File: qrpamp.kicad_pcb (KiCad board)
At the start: 2 copper layers, 144.8 x 82.6 mm, 110 parts, among them K1 BAND3_IN, K2 BAND2_IN, K3 BAND1_IN, K4 BAND3_OUT, K5 BAND2_OUT, K6 BAND1_OUT, K7 ANT_RLY, P1 PWR, P2 PWR_SW, P3 SWD, P4 ANT, P5 RADIO, P6 PTT_IN, P7 Thumb-Joystick, Q1 MMBT6427, Q2 MMBF170, Q3 IRF510, Q4 IRF510, SW1 SW_PUSH, T1 8:8, T2 8:8, T3 2:3, T4 12:1, T5 1:12, U1 LM7805, U2 LM3940, U3 LCD-2x16, U4 STM32F401xB/C-LQFP

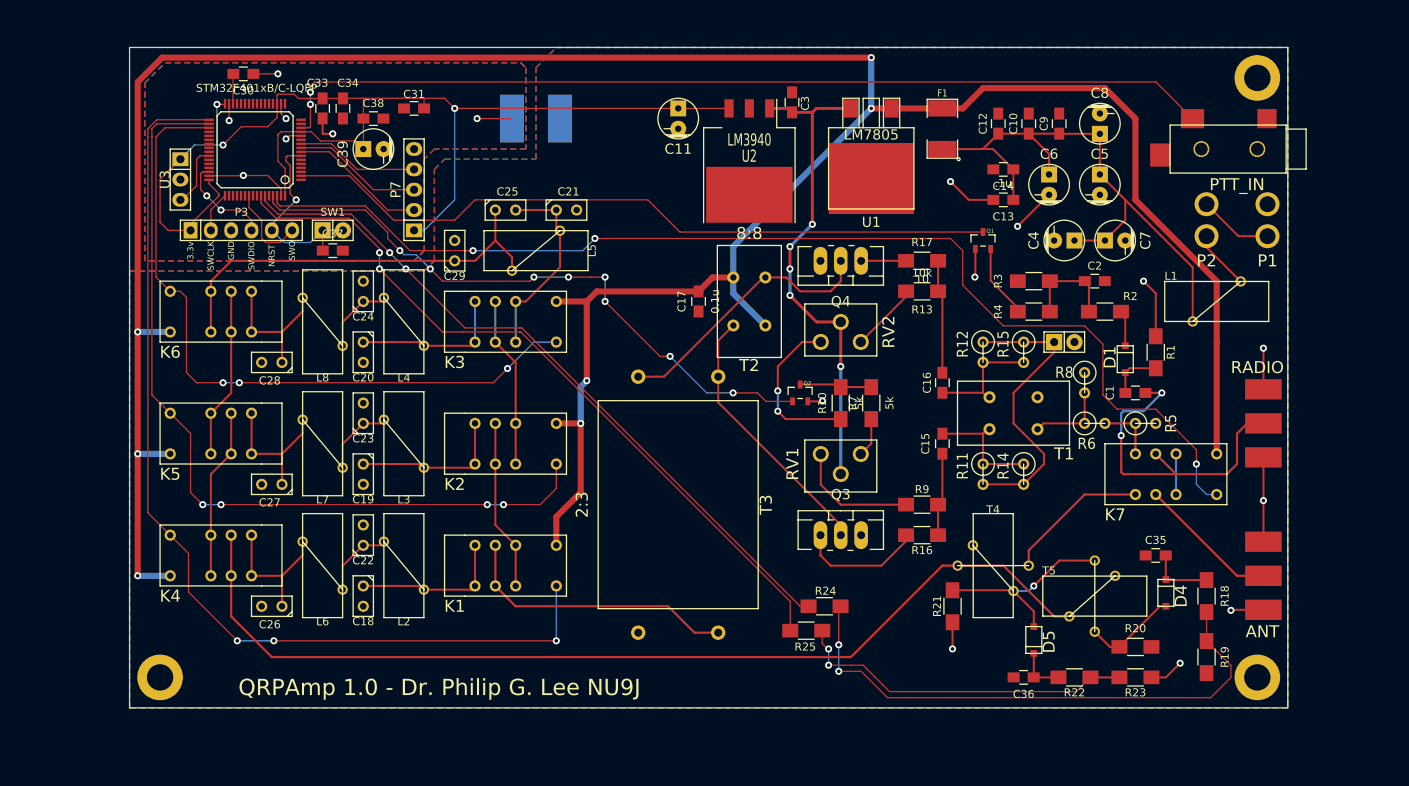
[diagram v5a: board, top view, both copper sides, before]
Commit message: Fixed issues found with test board
- Added MOSFETs to relay switch lines from MCU
- Reconnected SWR in/out to actual ADC pins
- Changed LM3940 footprint to SOT223
- Added 4th mounting hole
- Swapped joystick for nav button
- Extended pads of STM32F401 for easier soldering
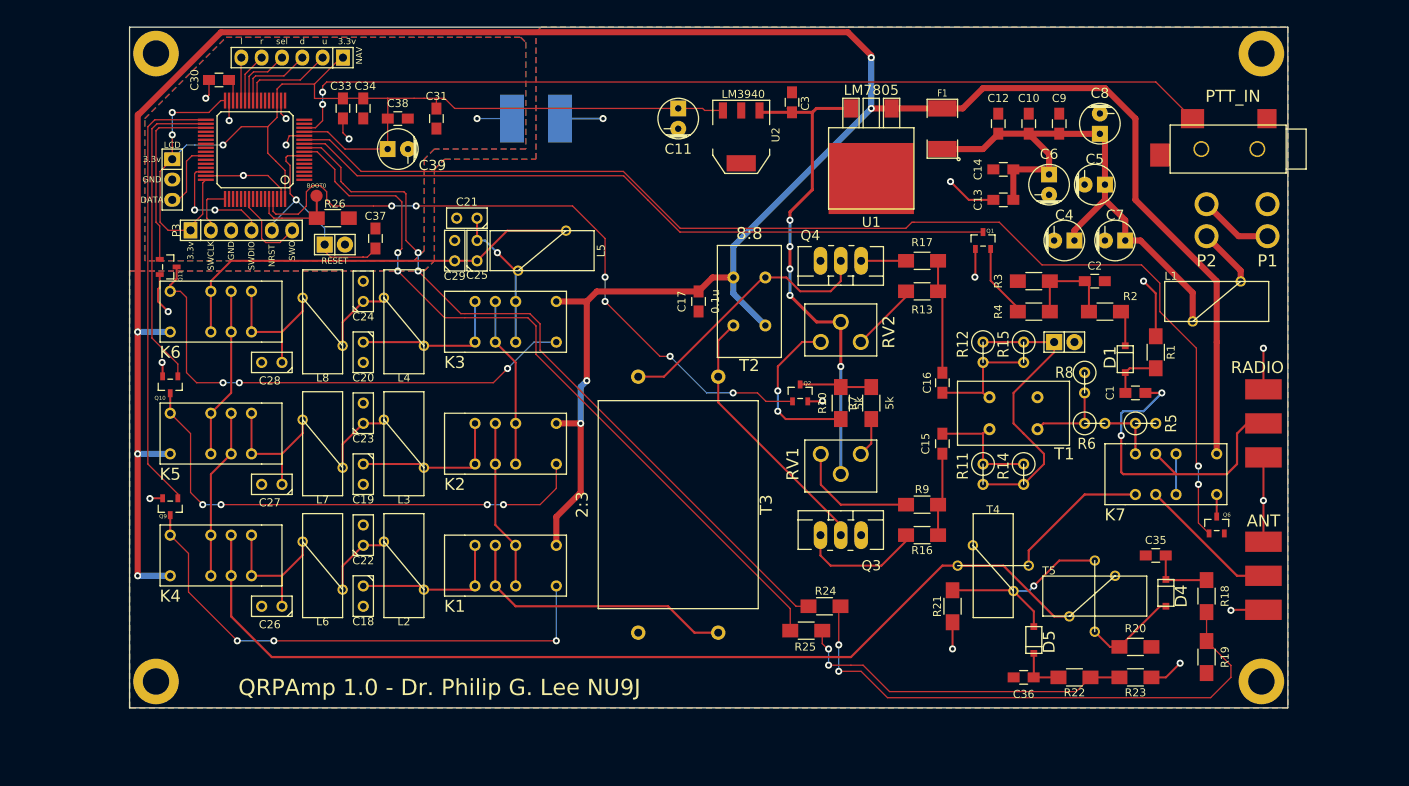
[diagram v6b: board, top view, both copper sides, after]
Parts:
- removed the Mounting Hole at (86.4, 128.3)
- removed the Mounting Hole at (223.5, 128.3)
- removed the Mounting Hole at (223.5, 53.3)
- added Mounting Hole: VAL**, nu9j-footprints:MountingHole4-40, F.Cu at (224.0, 53.3)
- added Mounting Hole: VAL**, nu9j-footprints:MountingHole4-40, F.Cu at (224.0, 128.8)
- added Mounting Hole: VAL**, nu9j-footprints:MountingHole4-40, F.Cu at (86.4, 128.8)
- added Mounting Hole: VAL**, nu9j-footprints:MountingHole4-40, F.Cu at (85.9, 50.3)
- added P8: NAV_BUTTON, Pin_Headers:Pin_Header_Straight_1x06, F.Cu at (102.9, 50.8)
- added Q10: MMBF170, nu9j-footprints:sot23-DGS, F.Cu at (87.6, 91.7)
- added Q11: MMBF170, nu9j-footprints:sot23-DGS, F.Cu at (87.4, 77.0)
- added Q6: MMBF170, nu9j-footprints:sot23-DGS, F.Cu at (218.4, 109.2)
- added Q9: MMBF170, nu9j-footprints:sot23-DGS, F.Cu at (87.6, 106.9)
- added R26: 10k, Resistors_SMD:R_1206_HandSoldering, F.Cu at (108.0, 70.9)
- P7: value Thumb-Joystick -> TP; footprint Pin_Headers:Pin_Header_Straight_1x05 -> Measurement_Points:Measurement_Point_Round-SMD-Pad_Small
- U2: footprint nu9j-footprints:TO-263_VIVOGND -> SMD_Packages:SOT-223
- moved C21 12.5 mm to (124.7, 70.9), turned to 180 degrees
- moved P7 12.2 mm to (105.9, 68.1)
- moved C25 6.20 mm to (126.0, 74.9), turned to 90 degrees
- moved C37 5.55 mm to (113.3, 73.4), turned to 90 degrees
- moved U2 3.70 mm to (159.0, 60.7)
- moved C30 3.14 mm to (93.7, 53.6), turned to 0 degrees
- moved C31 3.07 mm to (120.9, 58.4), turned to 270 degrees
- moved C38 3.05 mm to (116.1, 58.4)
- moved C39 3.05 mm to (116.1, 62.2)
- moved C34 2.54 mm to (111.8, 57.1)
- moved C33 2.54 mm to (109.2, 57.1)
- moved SW1 1.80 mm to (108.2, 74.2)
- moved U3 1.02 mm to (87.9, 66.0)
- moved L5 0.76 mm to (134.1, 74.9), turned to 90 degrees
- moved C5 0.64 mm to (203.2, 66.7), turned to 90 degrees
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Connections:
- K1 pad 12: /Band Filters/bandfilter_3sel -> /Band Filters/band3_sel
- K2 pad 12: /Band Filters/bandfilter_2sel -> /Band Filters/band2_sel
- K3 pad 12: /Band Filters/bandfilter_1sel -> /Band Filters/band1_sel
- K4 pad 12: /Band Filters/bandfilter_3sel -> /Band Filters/band3_sel
- K5 pad 12: /Band Filters/bandfilter_2sel -> /Band Filters/band2_sel
- K6 pad 12: /Band Filters/bandfilter_1sel -> /Band Filters/band1_sel
- K7 pad 12: /RF In/Out/ant_sw_rly -> Net-(K7-Pad12)
- P7 pad 1: +3.3V -> Net-(P7-Pad1)
- U4 pad 10: Net-(P7-Pad4) -> /Microcontroller/mcu_rfdet
- U4 pad 11: Net-(U4-Pad11) -> /RF In/Out/ant_sw_rly
- U4 pad 2: /Microcontroller/mcu_rfdet -> Net-(U4-Pad2)
- U4 pad 24: Net-(U4-Pad24) -> /Microcontroller/nav_up
- U4 pad 25: Net-(U4-Pad25) -> /Microcontroller/nav_down
- U4 pad 26: Net-(U4-Pad26) -> /Microcontroller/nav_select
- U4 pad 27: Net-(U4-Pad27) -> /Microcontroller/nav_right
- U4 pad 28: Net-(U4-Pad28) -> /Microcontroller/nav_left
- U4 pad 58: Net-(R24-Pad1) -> Net-(U4-Pad58)
- U4 pad 59: Net-(R25-Pad2) -> Net-(U4-Pad59)
- U4 pad 60: Net-(U4-Pad60) -> Net-(P7-Pad1)
- U4 pad 62: /RF In/Out/ant_sw_rly -> Net-(U4-Pad62)
- U4 pad 8: Net-(P7-Pad2) -> Net-(R24-Pad1)
- U4 pad 9: Net-(P7-Pad3) -> Net-(R25-Pad2)
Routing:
- net /Band Filters/bandfilter_3sel: track 123.5 -> 56.0 mm, vias 3 -> 0
- net /Band Filters/band3_sel: track 0.00 -> 65.9 mm, vias 0 -> 3
- net /Band Filters/bandfilter_2sel: track 105.1 -> 39.7 mm, vias 4 -> 0
- net /Band Filters/bandfilter_1sel: track 88.1 -> 23.0 mm, vias 3 -> 0
- net /Band Filters/band1_sel: track 0.00 -> 64.3 mm, vias 0 -> 3
- net /Band Filters/band2_sel: track 0.00 -> 63.7 mm, vias 0 -> 4
- net Net-(P7-Pad2): track 17.1 -> 0.00 mm
- net Net-(P7-Pad3): track 16.3 -> 0.00 mm
- net Net-(P7-Pad4): track 15.5 -> 0.00 mm
- net /Microcontroller/nav_up: track 0.00 -> 12.9 mm
- net Net-(P7-Pad1): track 0.00 -> 12.0 mm
- net /Microcontroller/nav_down: track 0.00 -> 11.3 mm
- net GND: track 52.2 -> 60.7 mm, vias 10 -> 13
- net /Microcontroller/nav_select: track 0.00 -> 8.11 mm
- net /Amplifier/amp_on: track 78.8 -> 85.5 mm, vias 8 -> 6
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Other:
- board size 144.8 x 82.6 mm -> 144.8 x 85.1 mm
- board text added: "BOOT0"
- board text added: "DATA"
- board text added: "LCD"
- board text added: "NAV"
- board text added: "RESET"
- board text added: "d"
- board text added: "l"
- board text added: "r"
- board text added: "sel"
- board text added: "u"

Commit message: Off to the fab!
Had to fix an issue where the GND-DGND bead was not putting solder
mask on the bottom pads.
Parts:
- L9: moved to B.Cu
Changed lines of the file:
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@@
     (links 250)
     (no_connects 0)
-    (area 82.474999 46.914999 227.405001 132.155001)
+    (area 80.118238 43.813 229.949001 132.155001)
     (thickness 1.6)
     (drawings 24)
@@
     (mod_text_size 1.5 1.5)
     (mod_text_width 0.15)
-    (pad_size 5.7 5.7)
-    (pad_drill 3.3)
+    (pad_size 2.99974 5.99948)
+    (pad_drill 0)
     (pad_to_mask_clearance 0.2)
     (aux_axis_origin 0 0)
@@
     (visible_elements FFFFFF7F)
     (pcbplotparams
-      (layerselection 0x00030_80000001)
+      (layerselection 0x000f0_80000001)
       (usegerberextensions false)
       (excludeedgelayer true)
@@
       (outputformat 1)
       (mirror false)
-      (drillshape 1)
+      (drillshape 0)
       (scaleselection 1)
-      (outputdirectory ""))
+      (outputdirectory gerber/))
   )
   (net 0 "")
@@
     (add_net "Net-(U3-Pad3)")
   )
+  (module nu9j-footprints:WE-SUCKW (layer B.Cu)
+    (at 133.35 58.42 180)
+    (fp_text reference L9 (at 0 5.00126 180) (layer B.SilkS)
+      (effects (font (thickness 0.3048)) (justify mirror))
+    )
+    (fp_text value BEAD (at 0 -5.00126 180) (layer B.SilkS)
+      (effects (font (thickness 0.3048)) (justify mirror))
+    )
+    (fp_line (start -5.99948 2.49936) (end -5.99948 -2.49936) (layer B.SilkS) (width 0.381))
+    (fp_line (start -5.99948 -2.49936) (end 5.99948 -2.49936) (layer B.SilkS) (width 0.381))
+    (fp_line (start 5.99948 -2.49936) (end 5.99948 2.49936) (layer B.SilkS) (width 0.381))
+    (fp_line (start 5.99948 2.49936) (end -5.99948 2.49936) (layer B.SilkS) (width 0.381))
+    (pad 1 smd rect (at -2.99974 0 180) (size 2.99974 5.99948) (layers B.Cu B.Paste B.Mask)
+      (net 3 GND))
+    (pad 2 smd rect (at 2.99974 0 180) (size 2.99974 5.99948) (layers B.Cu B.Paste B.Mask)
+      (net 88 DGND))
+  )
   (module nu9j-footprints:LQFP64 (layer F.Cu)
     (at 103.984 66.068143 90)
@@
       (net 34 "/Band Filters/bandfilter_out"))
   )
-  (module nu9j-footprints:WE-SUCKW (layer F.Cu)
-    (at 133.35 58.42 180)
-    (fp_text reference L9 (at 0 -5.00126 180) (layer B.SilkS)
-      (effects (font (thickness 0.3048)) (justify mirror))
-    )
-    (fp_text value BEAD (at 0 5.00126 180) (layer B.SilkS)
-      (effects (font (thickness 0.3048)) (justify mirror))
-    )
-    (fp_line (start -5.99948 -2.49936) (end -5.99948 2.49936) (layer B.SilkS) (width 0.381))
-    (fp_line (start -5.99948 2.49936) (end 5.99948 2.49936) (layer B.SilkS) (width 0.381))
-    (fp_line (start 5.99948 2.49936) (end 5.99948 -2.49936) (layer B.SilkS) (width 0.381))
-    (fp_line (start 5.99948 -2.49936) (end -5.99948 -2.49936) (layer B.SilkS) (width 0.381))
-    (pad 1 smd rect (at -2.99974 0 180) (size 2.99974 5.99948) (layers B.Cu F.Paste F.Mask)
-      (net 3 GND))
-    (pad 2 smd rect (at 2.99974 0 180) (size 2.99974 5.99948) (layers B.Cu F.Paste F.Mask)
-      (net 88 DGND))
-  )
   (module nu9j-footprints:TOROID-50 (layer F.Cu)

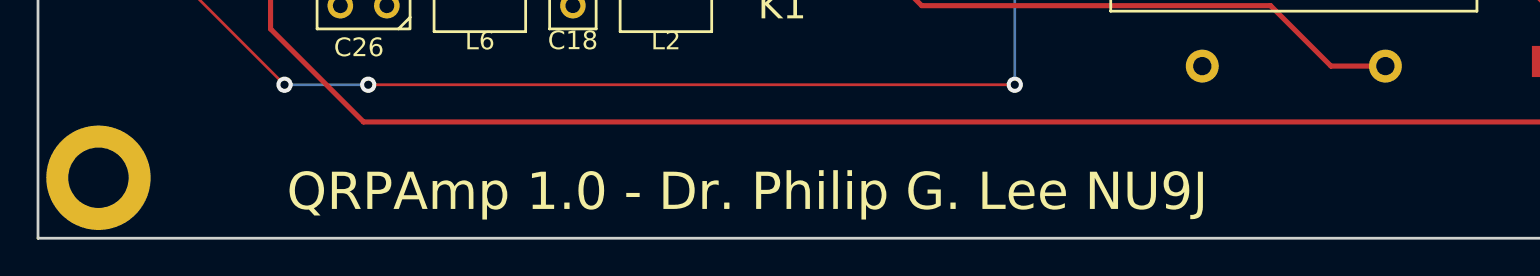
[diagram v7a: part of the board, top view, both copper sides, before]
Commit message: Put TAPR copyright notice on silkscreen
This fixes #1. Also, change "QRPAmp" to "ChibiAmp" on front silkscreen.
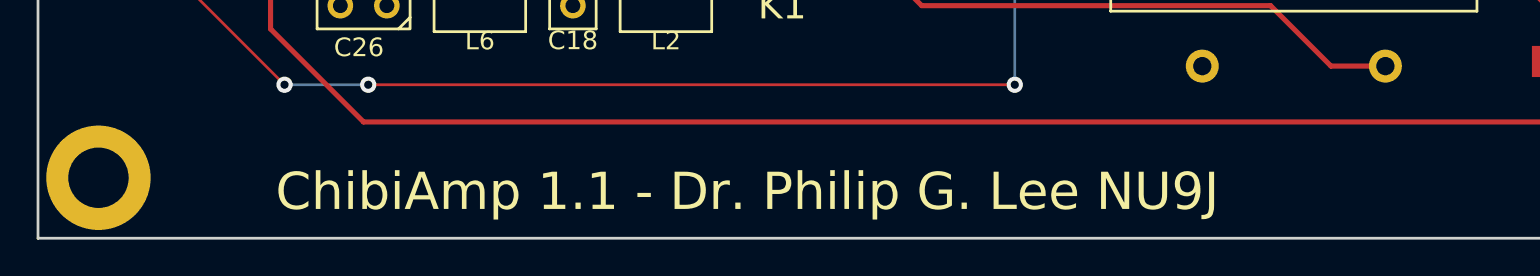
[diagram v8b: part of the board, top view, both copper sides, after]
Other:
- board text added: "ChibiAmp 1.1 - Dr. Philip G. Lee NU9J"
- board text added: "Copyright Philip G. Lee 2015. Licensed under the TAPR Open Hardware License version 1.0 (www.tapr.org/OHL)."
- board text removed: "QRPAmp 1.0 - Dr. Philip G. Lee NU9J"
